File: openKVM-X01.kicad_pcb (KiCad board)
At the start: 2 copper layers, 30 parts, among them J2 HDMI_A_1.4, J3 HDMI_A_1.4, SW1 SW_SPDT, U1 STM32F411VETx, U2 TS3DV642A0RUAR, Y1 Crystal

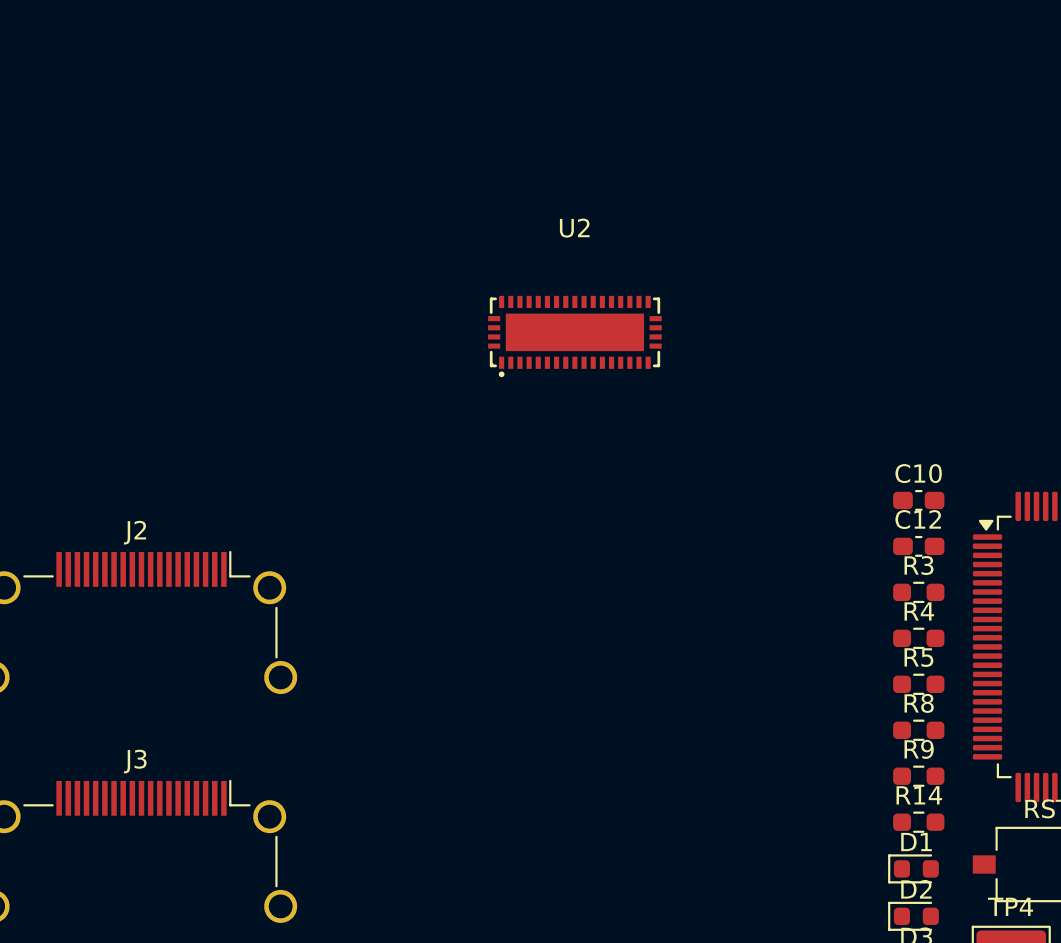
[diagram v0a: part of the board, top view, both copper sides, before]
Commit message: Created Branch and Made Changes
Fixed I2C going into Mux shorting the 3V3 side and 5V side due to nets being the same names. Added grounding to HDMI Out connector. Fixed footprint for TS3DV642A0RUAR to use KiCAD default library footprint with EasyEDA 3D model.
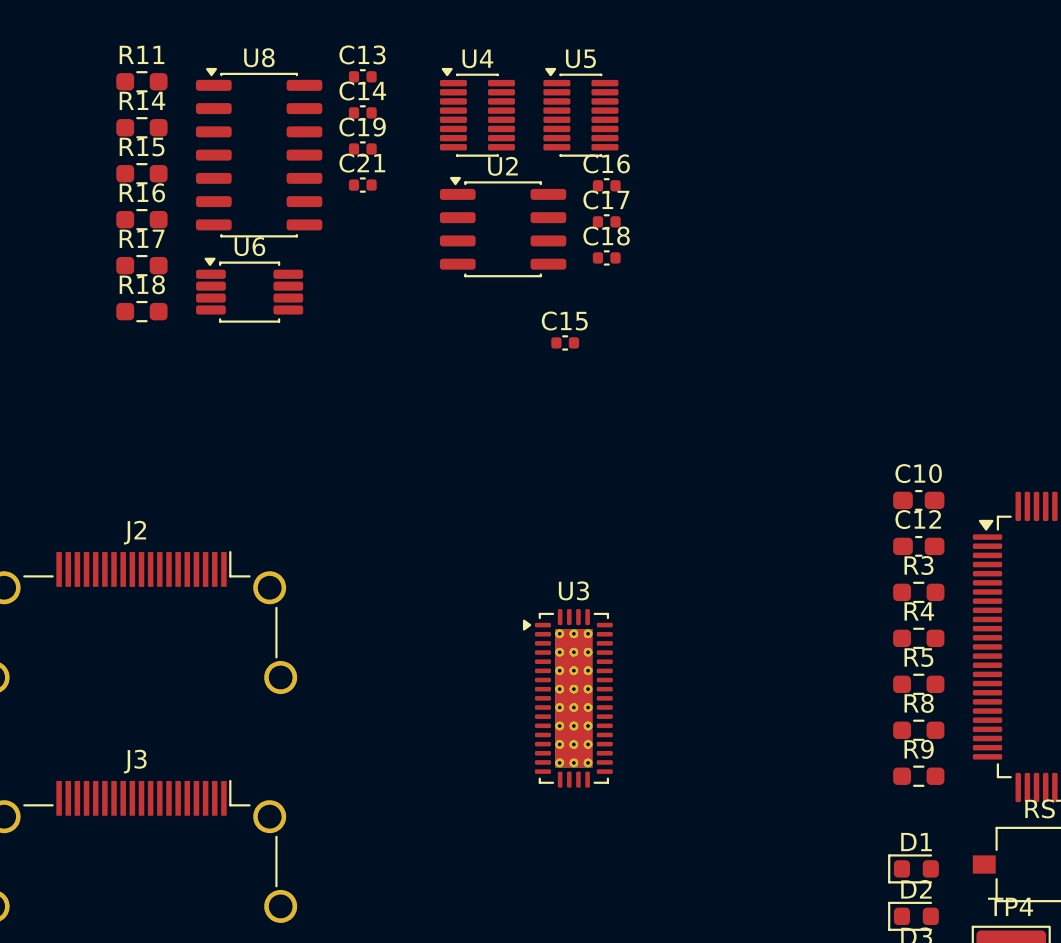
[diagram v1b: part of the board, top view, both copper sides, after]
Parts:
- added C13: 100nF, Capacitor_SMD:C_0402_1005Metric, F.Cu at (103.9, 27.2)
- added C14: 470nF, Capacitor_SMD:C_0402_1005Metric, F.Cu at (103.9, 29.1)
- added C15: 100nF, Capacitor_SMD:C_0402_1005Metric, F.Cu at (115.0, 41.7)
- added C16: 100nF, Capacitor_SMD:C_0402_1005Metric, F.Cu at (117.2, 33.1)
- added C17: 100nF, Capacitor_SMD:C_0402_1005Metric, F.Cu at (117.2, 35.1)
- added C18: 100nF, Capacitor_SMD:C_0402_1005Metric, F.Cu at (117.2, 37.0)
- added C19: 100nF, Capacitor_SMD:C_0402_1005Metric, F.Cu at (103.9, 31.1)
- added C21: 100nF, Capacitor_SMD:C_0402_1005Metric, F.Cu at (103.9, 33.1)
- added R11: 33, Resistor_SMD:R_0603_1608Metric_Pad0.98x0.95mm_HandSolder, F.Cu at (91.8, 27.4)
- added R15: 5K, Resistor_SMD:R_0603_1608Metric_Pad0.98x0.95mm_HandSolder, F.Cu at (91.8, 32.4)
- added R16: 10K, Resistor_SMD:R_0603_1608Metric_Pad0.98x0.95mm_HandSolder, F.Cu at (91.8, 35.0)
- added R17: 2K, Resistor_SMD:R_0603_1608Metric_Pad0.98x0.95mm_HandSolder, F.Cu at (91.8, 37.5)
- added R18: 2K, Resistor_SMD:R_0603_1608Metric_Pad0.98x0.95mm_HandSolder, F.Cu at (91.8, 40.0)
- added U3: TS3DV642A0RUAR, Package_DFN_QFN:WQFN-42-1EP_3.5x9mm_P0.5mm_EP2.05x7.55mm_ThermalVias, F.Cu at (115.4, 61.1)
- added U4: TMUX1574DYY, Package_SO:Texas_DYY0016A_TSOT-23-16_2x4.2mm_P0.5mm, F.Cu at (110.2, 29.2)
- added U5: TMUX1574DYY, Package_SO:Texas_DYY0016A_TSOT-23-16_2x4.2mm_P0.5mm, F.Cu at (115.8, 29.2)
- added U6: TCA9517ADGK, Package_SO:VSSOP-8_3x3mm_P0.65mm, F.Cu at (97.7, 38.9)
- added U8: 74HC7014, Package_SO:SOIC-14_3.9x8.7mm_P1.27mm, F.Cu at (98.2, 31.4)
- R14: value 220 -> 5K
- U2: value TS3DV642A0RUAR -> M24C02-RMN; footprint KiCadEasyEDA:WFQFN-42_L9.0-W3.5-P0.50-BL-EP -> Package_SO:SOIC-8_3.9x4.9mm_P1.27mm
- moved R14 56.9 mm to (91.8, 29.9)
- moved U2 6.86 mm to (111.6, 35.5)
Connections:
- net /Root/BOOT0 renamed /BOOT0
- net /Root/HDMI_1_OUT_CEC renamed /HDMI_1_OUT_CEC
- net /Root/HDMI_1_OUT_HPD renamed /HDMI_1_OUT_HPD
- net /Root/HDMI_1_OUT_UTIL renamed /HDMI_1_OUT_UTIL
- net /Root/HDMI_1_UTIL renamed /HDMI_1_UTIL
- net /Root/NRST renamed /NRST
- net Net-(U1-PH0) renamed /MCU_OSC_IN
- C8 pad 1: /Root/MCU_OSC_OUT_B -> /MCU_OSC_OUT
- J2 pad 1: /Root/HDMI_1_D2+ -> /HDMI_1_D2+
- J2 pad 10: /Root/HDMI_1_Ck+ -> /HDMI_1_CK+
- J2 pad 11: unconnected-(J2-CKS-Pad11) -> GND
- J2 pad 12: /Root/HDMI_1_CK- -> /HDMI_1_CK-
- J2 pad 13: /Root/HDMI_1_CEC -> /HDMI_1_CEC
- J2 pad 15: /Root/HDMI_1_SCK -> /HDMI_1_SCK
- J2 pad 16: /Root/HDMI_1_SDA -> /HDMI_1_SDA
- J2 pad 17: unconnected-(J2-GND-Pad17) -> GND
- J2 pad 19: /Root/HDMI_1_HPD -> /HDMI_1_HPD
- J2 pad 2: unconnected-(J2-D2S-Pad2) -> GND
- J2 pad 3: /Root/HDMI_1_D2- -> /HDMI_1_D2-
- J2 pad 4: /Root/HDMI_1_D1+ -> /HDMI_1_D1+
- J2 pad 5: unconnected-(J2-D1S-Pad5) -> GND
- J2 pad 6: /Root/HDMI_1_D1- -> /HDMI_1_D1-
- J2 pad 7: /Root/HDMI_1_D0+ -> /HDMI_1_D0+
- J2 pad 8: unconnected-(J2-D0S-Pad8) -> GND
- J2 pad 9: /Root/HDMI_1_D0- -> /HDMI_1_D0-
- J2 pad SH: unconnected-(J2-PadSH) -> GND
- J3 pad 1: /Root/HDMI_1_OUT_D2+ -> /HDMI_1_OUT_D2+
- J3 pad 10: /Root/HDMI_1_OUT_Ck+ -> /HDMI_1_OUT_Ck+
- J3 pad 12: /Root/HDMI_1_OUT_CK- -> /HDMI_1_OUT_CK-
- J3 pad 15: /Root/HDMI_1_OUT_SCK -> /HDMI_1_OUT_SCK
- J3 pad 16: /Root/HDMI_1_OUT_SDA -> /HDMI_1_OUT_SDA
- J3 pad 3: /Root/HDMI_1_OUT_D2- -> /HDMI_1_OUT_D2-
- J3 pad 4: /Root/HDMI_1_OUT_D1+ -> /HDMI_1_OUT_D1+
- J3 pad 6: /Root/HDMI_1_OUT_D1- -> /HDMI_1_OUT_D1-
- J3 pad 7: /Root/HDMI_1_OUT_D0+ -> /HDMI_1_OUT_D0+
- J3 pad 9: /Root/HDMI_1_OUT_D0- -> /HDMI_1_OUT_D0-
- R14 pad 1: /Root/MCU_OSC_OUT_B -> /uC_I2C1_SCL
- R14 pad 2: Net-(U1-PH1) -> +3V3
- U1 pad 13: Net-(U1-PH1) -> /MCU_OSC_OUT
- U1 pad 15: unconnected-(U1-PC0-Pad15) -> /HDMI_COM_SEL
- U1 pad 16: unconnected-(U1-PC1-Pad16) -> /HDMI_MUX_EN
- U1 pad 17: unconnected-(U1-PC2-Pad17) -> /HDMI_TCA_EN
- U1 pad 82: unconnected-(U1-PD1-Pad82) -> Net-(U1-PD1)
- U1 pad 92: unconnected-(U1-PB6-Pad92) -> /uC_I2C1_SCL
- U1 pad 93: unconnected-(U1-PB7-Pad93) -> /uC_I2C1_SDA
- U2 pad 4: unconnected-(U2-SDA-Pad4) -> GND
- U2 pad 5: unconnected-(U2-D0+-Pad5) -> Net-(U2-SDA)
- U2 pad 6: unconnected-(U2-D0--Pad6) -> Net-(U2-SCL)
- U2 pad 8: unconnected-(U2-D1--Pad8) -> 5V
- Y1 pad 1: /Root/MCU_OSC_OUT_B -> /MCU_OSC_OUT

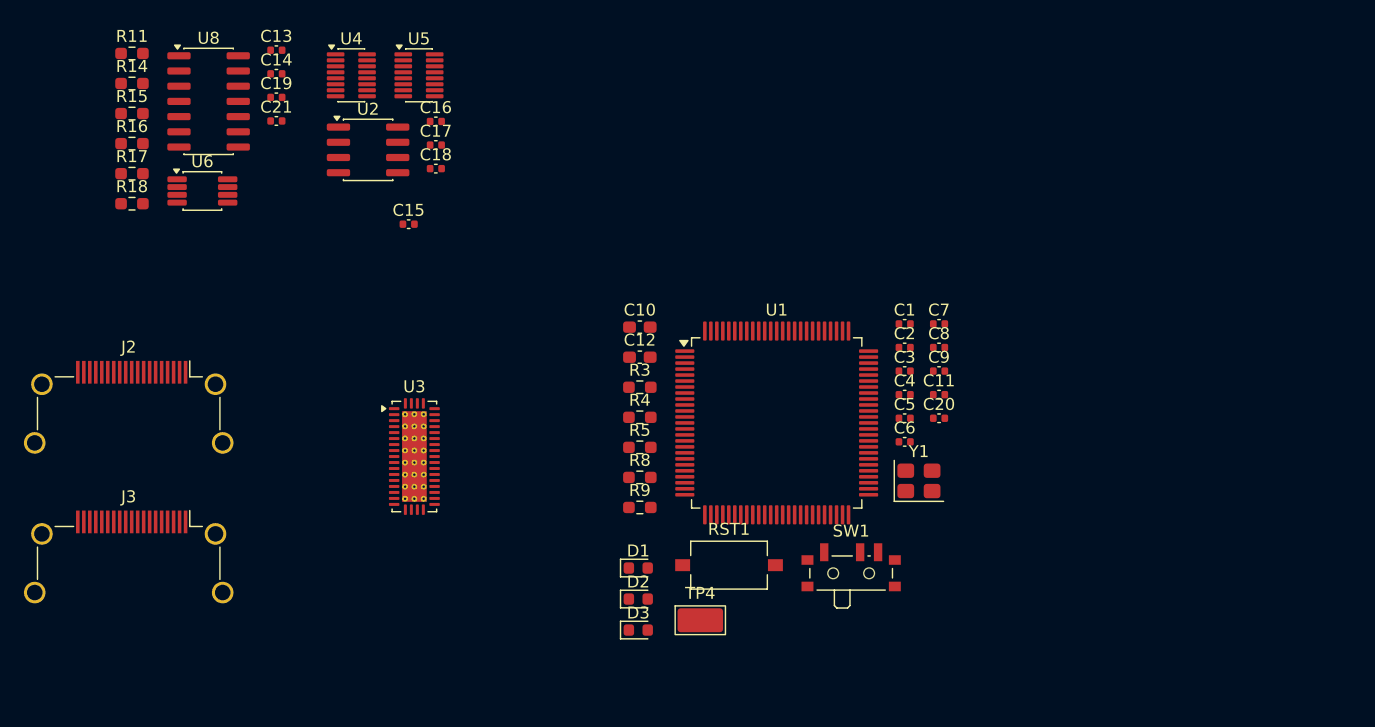
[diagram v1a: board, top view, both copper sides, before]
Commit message: Rearranged Project
Rearranged project pages to have a block diagram and upper level collector for all future hierarchical pages to be collected under when adding power pages. Started on Power conversion with 12V input jack.
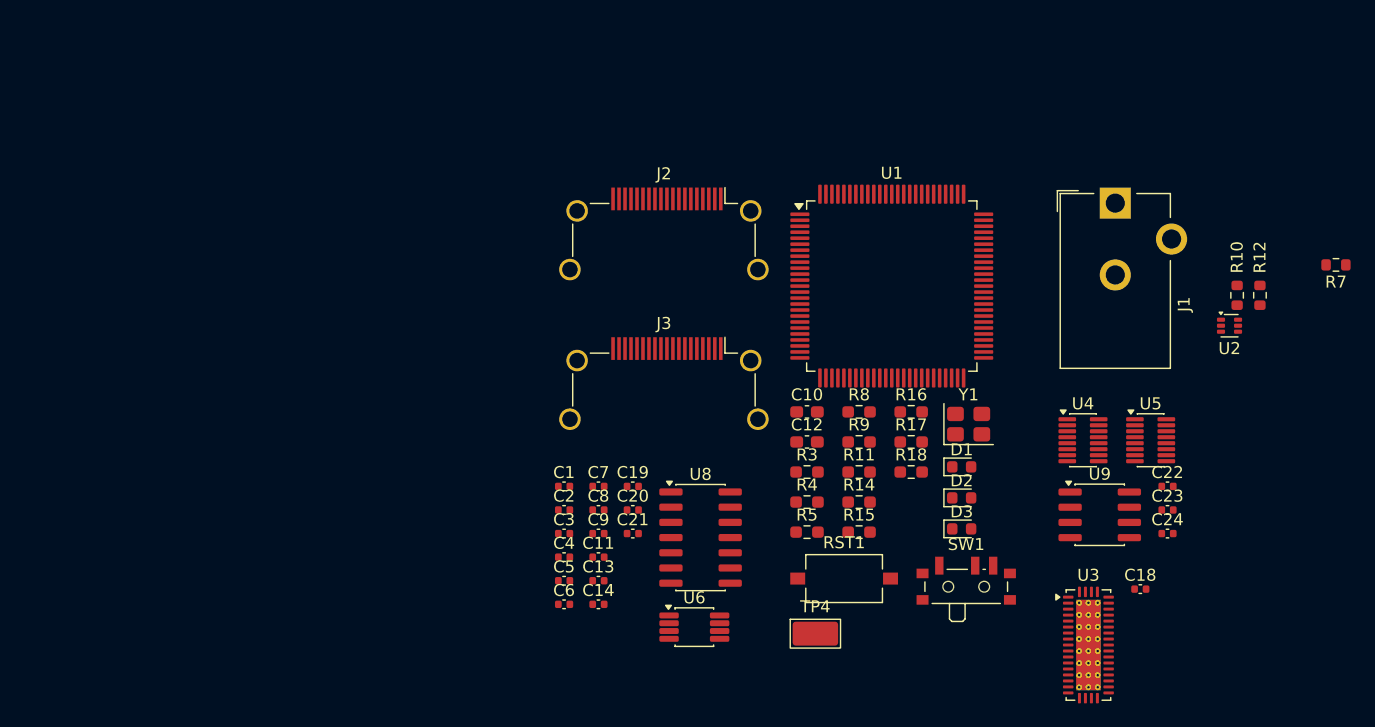
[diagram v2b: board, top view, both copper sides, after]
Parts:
- removed C15, C16, C17: 100nF, Capacitor_SMD:C_0402_1005Metric
- added C22: 100nF, Capacitor_SMD:C_0402_1005Metric, F.Cu at (178.3, 63.6)
- added C23: 100nF, Capacitor_SMD:C_0402_1005Metric, F.Cu at (178.3, 65.6)
- added C24: 100nF, Capacitor_SMD:C_0402_1005Metric, F.Cu at (178.3, 67.5)
- added J1: PJ-102AH, Connector_BarrelJack:BarrelJack_CUI_PJ-102AH_Horizontal, F.Cu at (174.0, 39.9)
- added R10: R, Resistor_SMD:R_0603_1608Metric, F.Cu at (184.2, 47.6)
- added R12: R, Resistor_SMD:R_0603_1608Metric, F.Cu at (186.1, 47.6)
- added R7: 10k, Resistor_SMD:R_0603_1608Metric, F.Cu at (192.4, 45.1)
- added U9: M24C02-RMN, Package_SO:SOIC-8_3.9x4.9mm_P1.27mm, F.Cu at (172.7, 66.0)
- U2: value M24C02-RMN -> TPS562242B; footprint Package_SO:SOIC-8_3.9x4.9mm_P1.27mm -> Package_TO_SOT_SMD:SOT-563
- moved U2 73.4 mm to (183.5, 50.2)
- moved R11 70.1 mm to (152.6, 62.4)
- moved R14 70.1 mm to (152.6, 64.9)
- moved R15 70.1 mm to (152.6, 67.4)
- moved R16 68.8 mm to (156.9, 57.4)
- moved R17 68.8 mm to (156.9, 59.9)
- moved R18 68.8 mm to (156.9, 62.4)
- moved C18 68.5 mm to (176.1, 72.2)
- moved U5 68.3 mm to (176.9, 59.7)
- moved U4 68.3 mm to (171.3, 59.7)
- moved U3 58.5 mm to (171.7, 76.8)
- moved U6 54.9 mm to (138.8, 75.3)
- moved U8 54.9 mm to (139.3, 67.9)
- moved C13 51.8 mm to (130.8, 71.5)
- moved C14 51.8 mm to (130.8, 73.4)
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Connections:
- net /BOOT0 renamed /ProjectArchitecture/HDMI/BOOT0
- net /EDID_EMULATION/COM1_EDID_EMU_SCL renamed /ProjectArchitecture/HDMI/EDID_EMULATION/COM1_EDID_EMU_SCL
- net /EDID_EMULATION/COM1_EDID_EMU_SDA renamed /ProjectArchitecture/HDMI/EDID_EMULATION/COM1_EDID_EMU_SDA
- net /EDID_EMULATION/uC_I2C1_SCL renamed /ProjectArchitecture/HDMI/EDID_EMULATION/5V_uC_I2C1_SCL
- net /EDID_EMULATION/uC_I2C1_SDA renamed /ProjectArchitecture/HDMI/EDID_EMULATION/5V_uC_I2C1_SDA
- net /HDMI_1_CEC renamed /ProjectArchitecture/HDMI/HDMI_1_CEC
- net /HDMI_1_CK+ renamed /ProjectArchitecture/HDMI/HDMI_1_CK+
- net /HDMI_1_CK- renamed /ProjectArchitecture/HDMI/HDMI_1_CK-
- net /HDMI_1_D0+ renamed /ProjectArchitecture/HDMI/HDMI_1_D0+
- net /HDMI_1_D0- renamed /ProjectArchitecture/HDMI/HDMI_1_D0-
- net /HDMI_1_D1+ renamed /ProjectArchitecture/HDMI/HDMI_1_D1+
- net /HDMI_1_D1- renamed /ProjectArchitecture/HDMI/HDMI_1_D1-
- net /HDMI_1_D2+ renamed /ProjectArchitecture/HDMI/HDMI_1_D2+
- net /HDMI_1_D2- renamed /ProjectArchitecture/HDMI/HDMI_1_D2-
- net /HDMI_1_HPD renamed /ProjectArchitecture/HDMI/HDMI_1_HPD
- net /HDMI_1_OUT_CEC renamed /ProjectArchitecture/HDMI/HDMI_1_OUT_CEC
- net /HDMI_1_OUT_CK- renamed /ProjectArchitecture/HDMI/HDMI_1_OUT_CK-
- net /HDMI_1_OUT_Ck+ renamed /ProjectArchitecture/HDMI/HDMI_1_OUT_Ck+
- net /HDMI_1_OUT_D0+ renamed /ProjectArchitecture/HDMI/HDMI_1_OUT_D0+
- net /HDMI_1_OUT_D0- renamed /ProjectArchitecture/HDMI/HDMI_1_OUT_D0-
- net /HDMI_1_OUT_D1+ renamed /ProjectArchitecture/HDMI/HDMI_1_OUT_D1+
- net /HDMI_1_OUT_D1- renamed /ProjectArchitecture/HDMI/HDMI_1_OUT_D1-
- net /HDMI_1_OUT_D2+ renamed /ProjectArchitecture/HDMI/HDMI_1_OUT_D2+
- net /HDMI_1_OUT_D2- renamed /ProjectArchitecture/HDMI/HDMI_1_OUT_D2-
- net /HDMI_1_OUT_HPD renamed /ProjectArchitecture/HDMI/HDMI_1_OUT_HPD
- net /HDMI_1_OUT_SCK renamed /ProjectArchitecture/HDMI/HDMI_1_OUT_SCK
- net /HDMI_1_OUT_SDA renamed /ProjectArchitecture/HDMI/HDMI_1_OUT_SDA
- net /HDMI_1_OUT_UTIL renamed /ProjectArchitecture/HDMI/HDMI_1_OUT_UTIL
- net /HDMI_1_SCK renamed /ProjectArchitecture/HDMI/HDMI_1_SCK
- net /HDMI_1_SDA renamed /ProjectArchitecture/HDMI/HDMI_1_SDA
- net /HDMI_1_UTIL renamed /ProjectArchitecture/HDMI/HDMI_1_UTIL
- net /HDMI_COM_SEL renamed /ProjectArchitecture/HDMI/HDMI_COM_SEL
- net /HDMI_COM_SELECT renamed /ProjectArchitecture/HDMI/HDMI_COM_SELECT
- net /HDMI_MUX/HDMI_1_OUT_CEC renamed /ProjectArchitecture/HDMI/HDMI_MUX/HDMI_1_OUT_CEC
- net /HDMI_MUX_EN renamed /ProjectArchitecture/HDMI/HDMI_MUX_EN
- net /HDMI_TCA_EN renamed /ProjectArchitecture/HDMI/HDMI_TCA_EN
- net /MCU_OSC_IN renamed /ProjectArchitecture/HDMI/MCU_OSC_IN
- net /MCU_OSC_OUT renamed /ProjectArchitecture/HDMI/MCU_OSC_OUT
- net /NRST renamed /ProjectArchitecture/HDMI/NRST
- net /uC_I2C1_SCL renamed /ProjectArchitecture/HDMI/uC_I2C1_SCL
- net /uC_I2C1_SDA renamed /ProjectArchitecture/HDMI/uC_I2C1_SDA
- C18 pad 1: 5V -> +3V3
- J3 pad 11: unconnected-(J3-CKS-Pad11) -> GND
- J3 pad 17: unconnected-(J3-GND-Pad17) -> GND
- J3 pad 2: unconnected-(J3-D2S-Pad2) -> GND
- J3 pad 5: unconnected-(J3-D1S-Pad5) -> GND
- J3 pad 8: unconnected-(J3-D0S-Pad8) -> GND
- J3 pad SH: unconnected-(J3-PadSH) -> GND
- U2 pad 1: unconnected-(U2-E0-Pad1) -> +12V
- U2 pad 2: unconnected-(U2-E1-Pad2) -> /ProjectArchitecture/POWER/U2_SW
- U2 pad 3: unconnected-(U2-E2-Pad3) -> GND
- U2 pad 4: GND -> /ProjectArchitecture/POWER/U2_BST
- U2 pad 5: Net-(U2-SDA) -> /ProjectArchitecture/POWER/U2_EN
- U2 pad 6: Net-(U2-SCL) -> /ProjectArchitecture/POWER/U2_FB
- U5 pad 4: Net-(U2-SDA) -> Net-(U5-D1)
- U5 pad 7: Net-(U2-SCL) -> Net-(U5-D2)
